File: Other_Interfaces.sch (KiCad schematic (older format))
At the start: 1 part, among them J9 2908-05WB-MG

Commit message: Add uSD circuitry
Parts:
- added C? (x2): C_100n_0402, antmicro-footprints:0402-cap, symbol antmicroCapacitors0402:C_100n_0402
- added C?: C_10u_0603, antmicro-footprints:0603-cap, symbol antmicroCapacitors0603:C_10u_0603
- added D? (x2): TPD4E05U06_PASS, antmicro-footprints:TPD4E05U06_PASS, symbol antmicroTVSDiodes:TPD4E05U06_PASS
- added IC?: AP22652W6-7, antmicro-footprints:SOT-23-6, symbol antmicroPMICPowerDistributionSwitchesLoadDrivers:AP22652W6-7
- added R?: R_20k_0402, antmicro-footprints:0402-res, symbol antmicroResistors0402:R_20k_0402
- added R?: R_10k_0402, antmicro-footprints:0402-res, symbol antmicroResistors0402:R_10k_0402
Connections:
- net labels added: 3V3, GND, SDMCC_EN, SDMCC_VDD, SDMCC_VDD_FAULT#, SDMCC_VDD_ILIM, SDMMC_CD, SDMMC_CLK, SDMMC_CMD, SDMMC_DAT0, SDMMC_DAT1, SDMMC_DAT2, SDMMC_DAT3
- wire segments 0 -> 50
- no-connect marks 0 -> 1
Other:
- note added: "Text"
- note removed: "Work in progress."
- moved on the sheet: J9

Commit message: Annotate parts in Other_Interfaces.sch
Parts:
- gave numbers to parts that had none: 8
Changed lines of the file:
@@
 Text
 $Comp
-L antmicroTVSDiodes:TPD4E05U06_PASS D?
+L antmicroTVSDiodes:TPD4E05U06_PASS D21
 U 1 1 61F2105E
 P 2450 3650
-F 0 "D?" V 2933 3600 60  0000 C CNN
+F 0 "D21" V 2933 3600 60  0000 C CNN
 F 1 "TPD4E05U06_PASS" V 3039 3600 60  0000 C CNN
 F 2 "antmicro-footprints:TPD4E05U06_PASS" H 2450 3650 60  0001 C CNN
@@
 $EndComp
 $Comp
-L antmicroTVSDiodes:TPD4E05U06_PASS D?
+L antmicroTVSDiodes:TPD4E05U06_PASS D22
 U 1 1 61F22664
 P 3375 3650
-F 0 "D?" V 3858 3600 60  0000 C CNN
+F 0 "D22" V 3858 3600 60  0000 C CNN
 F 1 "TPD4E05U06_PASS" V 3964 3600 60  0000 C CNN
 F 2 "antmicro-footprints:TPD4E05U06_PASS" H 3375 3650 60  0001 C CNN
@@
 $EndComp
 $Comp
-L antmicroPMICPowerDistributionSwitchesLoadDrivers:AP22652W6-7 IC?
+L antmicroPMICPowerDistributionSwitchesLoadDrivers:AP22652W6-7 IC2
 U 1 1 61F28646
 P 2400 1450
-F 0 "IC?" H 2400 1815 50  0000 C CNN
+F 0 "IC2" H 2400 1815 50  0000 C CNN
 F 1 "AP22652W6-7" H 2400 1724 50  0000 C CNN
 F 2 "antmicro-footprints:SOT-23-6" H 2400 1200 50  0001 C CNN
@@
 P 1950 1600
 AR Path="/61A60486/61F34FAA" Ref="#PWR?"  Part="1"
-AR Path="/61C01D88/61F34FAA" Ref="#PWR?"  Part="1"
-F 0 "#PWR?" H 1950 1350 50  0001 C CNN
+AR Path="/61C01D88/61F34FAA" Ref="#PWR0184"  Part="1"
+F 0 "#PWR0184" H 1950 1350 50  0001 C CNN
 F 1 "GND" H 1955 1427 50  0000 C CNN
 F 2 "" H 1950 1600 50  0001 C CNN
@@
 	2800 1350 3175 1350
 $Comp
-L antmicroCapacitors0402:C_100n_0402 C?
+L antmicroCapacitors0402:C_100n_0402 C124
 U 1 1 61F42291
 P 1400 1500
-F 0 "C?" H 1515 1455 60  0000 L CNN
+F 0 "C124" H 1515 1455 60  0000 L CNN
 F 1 "C_100n_0402" H 1400 1350 60  0001 C CNN
 F 2 "antmicro-footprints:0402-cap" H 1600 1700 60  0001 L CNN
@@
 P 1400 1650
 AR Path="/61A60486/61F43E22" Ref="#PWR?"  Part="1"
-AR Path="/61C01D88/61F43E22" Ref="#PWR?"  Part="1"
-F 0 "#PWR?" H 1400 1400 50  0001 C CNN
+AR Path="/61C01D88/61F43E22" Ref="#PWR0185"  Part="1"
+F 0 "#PWR0185" H 1400 1400 50  0001 C CNN
 F 1 "GND" H 1405 1477 50  0000 C CNN
 F 2 "" H 1400 1650 50  0001 C CNN
@@
 	2850 1550 2850 1600
 $Comp
-L antmicroResistors0402:R_20k_0402 R?
+L antmicroResistors0402:R_20k_0402 R105
 U 1 1 61F44F3A
 P 2850 1750
-F 0 "R?" V 2805 1820 60  0000 L CNN
+F 0 "R105" V 2805 1820 60  0000 L CNN
 F 1 "R_20k_0402" H 2850 1600 60  0001 C CNN
 F 2 "antmicro-footprints:0402-res" H 3050 1950 60  0001 L CNN
@@
 P 2850 1900
 AR Path="/61A60486/61F45C55" Ref="#PWR?"  Part="1"
-AR Path="/61C01D88/61F45C55" Ref="#PWR?"  Part="1"
-F 0 "#PWR?" H 2850 1650 50  0001 C CNN
+AR Path="/61C01D88/61F45C55" Ref="#PWR0186"  Part="1"
+F 0 "#PWR0186" H 2850 1650 50  0001 C CNN
 F 1 "GND" H 2855 1727 50  0000 C CNN
 F 2 "" H 2850 1900 50  0001 C CNN
@@
 $EndComp
 $Comp
-L antmicroResistors0402:R_10k_0402 R?
+L antmicroResistors0402:R_10k_0402 R104
 U 1 1 61F474AB
 P 2850 1125
-F 0 "R?" V 2805 1195 60  0000 L CNN
+F 0 "R104" V 2805 1195 60  0000 L CNN
 F 1 "R_10k_0402" H 2850 975 60  0001 C CNN
 F 2 "antmicro-footprints:0402-res" H 3050 1325 60  0001 L CNN
@@
 	2850 925  2850 975
 $Comp
-L antmicroCapacitors0402:C_100n_0402 C?
+L antmicroCapacitors0402:C_100n_0402 C125
 U 1 1 61F4A017
 P 3175 1500
-F 0 "C?" H 3060 1455 60  0000 R CNN
+F 0 "C125" H 3060 1455 60  0000 R CNN
 F 1 "C_100n_0402" H 3175 1350 60  0001 C CNN
 F 2 "antmicro-footprints:0402-cap" H 3375 1700 60  0001 L CNN
@@
 P 3175 1650
 AR Path="/61A60486/61F4A01D" Ref="#PWR?"  Part="1"
-AR Path="/61C01D88/61F4A01D" Ref="#PWR?"  Part="1"
-F 0 "#PWR?" H 3175 1400 50  0001 C CNN
+AR Path="/61C01D88/61F4A01D" Ref="#PWR0187"  Part="1"
+F 0 "#PWR0187" H 3175 1400 50  0001 C CNN
 F 1 "GND" H 3180 1477 50  0000 C CNN
 F 2 "" H 3175 1650 50  0001 C CNN
@@
 	3175 1350 3350 1350
 $Comp
-L antmicroCapacitors0603:C_10u_0603 C?
+L antmicroCapacitors0603:C_10u_0603 C126
 U 1 1 61F4D677
 P 3650 1500
-F 0 "C?" H 3765 1545 60  0000 L CNN
+F 0 "C126" H 3765 1545 60  0000 L CNN
 F 1 "C_10u_0603" H 3650 1350 60  0001 C CNN
 F 2 "antmicro-footprints:0603-cap" H 3850 1700 60  0001 L CNN
@@
 P 3650 1650
 AR Path="/61A60486/61F4E5D5" Ref="#PWR?"  Part="1"
-AR Path="/61C01D88/61F4E5D5" Ref="#PWR?"  Part="1"
-F 0 "#PWR?" H 3650 1400 50  0001 C CNN
+AR Path="/61C01D88/61F4E5D5" Ref="#PWR0188"  Part="1"
+F 0 "#PWR0188" H 3650 1400 50  0001 C CNN
 F 1 "GND" H 3655 1477 50  0000 C CNN
 F 2 "" H 3650 1650 50  0001 C CNN
@@
 AR Path="/61B0DC30/61F53284" Ref="#FLG?"  Part="1"
 AR Path="/61DC2BE0/61F53284" Ref="#FLG?"  Part="1"
-F 0 "#FLG?" H 3350 1425 50  0001 C CNN
+AR Path="/61C01D88/61F53284" Ref="#FLG0107"  Part="1"
+F 0 "#FLG0107" H 3350 1425 50  0001 C CNN
 F 1 "PWR_FLAG" H 3350 1523 50  0000 C CNN
 F 2 "" H 3350 1350 50  0001 C CNN
@@
 P 1950 3575
 AR Path="/61A60486/61F64597" Ref="#PWR?"  Part="1"
-AR Path="/61C01D88/61F64597" Ref="#PWR?"  Part="1"
-F 0 "#PWR?" H 1950 3325 50  0001 C CNN
+AR Path="/61C01D88/61F64597" Ref="#PWR0189"  Part="1"
+F 0 "#PWR0189" H 1950 3325 50  0001 C CNN
 F 1 "GND" H 1955 3402 50  0000 C CNN
 F 2 "" H 1950 3575 50  0001 C CNN
@@
 P 2875 3575
 AR Path="/61A60486/61F649BB" Ref="#PWR?"  Part="1"
-AR Path="/61C01D88/61F649BB" Ref="#PWR?"  Part="1"
-F 0 "#PWR?" H 2875 3325 50  0001 C CNN
+AR Path="/61C01D88/61F649BB" Ref="#PWR0190"  Part="1"
+F 0 "#PWR0190" H 2875 3325 50  0001 C CNN
 F 1 "GND" H 2880 3402 50  0000 C CNN
 F 2 "" H 2875 3575 50  0001 C CNN
@@
 P 4050 3350
 AR Path="/61A60486/61F78331" Ref="#PWR?"  Part="1"
-AR Path="/61C01D88/61F78331" Ref="#PWR?"  Part="1"
-F 0 "#PWR?" H 4050 3100 50  0001 C CNN
+AR Path="/61C01D88/61F78331" Ref="#PWR0191"  Part="1"
+F 0 "#PWR0191" H 4050 3100 50  0001 C CNN
 F 1 "GND" H 4055 3177 50  0000 C CNN
 F 2 "" H 4050 3350 50  0001 C CNN

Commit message: Connect uSD to SOM
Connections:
- net labels added: SD_CLK, SD_CMD, SD_DATA0, SD_DATA1, SD_DATA2, SD_DATA3, SD_DET
- net labels removed: SDMMC_CD, SDMMC_CLK, SDMMC_CMD, SDMMC_DAT0, SDMMC_DAT1, SDMMC_DAT2, SDMMC_DAT3
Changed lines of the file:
@@
 	1    0    0    -1
 $EndComp
-Text GLabel 1625 3200 0    50   Input ~ 0
-SDMMC_DAT1
-Text GLabel 1625 3100 0    50   Input ~ 0
-SDMMC_DAT0
-Text GLabel 1625 2500 0    50   Input ~ 0
-SDMMC_DAT2
-Text GLabel 1625 2600 0    50   Input ~ 0
-SDMMC_DAT3
-Text GLabel 1625 2700 0    50   Input ~ 0
-SDMMC_CMD
-Text GLabel 1625 2900 0    50   Input ~ 0
-SDMMC_CLK
-Text GLabel 1625 2400 0    50   Input ~ 0
-SDMMC_CD
 Wire Wire Line
 	4100 3300 4050 3300
@@
 Wire Wire Line
 	3350 1350 3650 1350
+Text GLabel 1625 2900 0    50   Input ~ 0
+SD_CLK
+Text GLabel 1625 2700 0    50   Input ~ 0
+SD_CMD
+Text GLabel 1625 2400 0    50   Input ~ 0
+SD_DET
+Text GLabel 1625 3100 0    50   Input ~ 0
+SD_DATA0
+Text GLabel 1625 3200 0    50   Input ~ 0
+SD_DATA1
+Text GLabel 1625 2600 0    50   Input ~ 0
+SD_DATA3
+Text GLabel 1625 2500 0    50   Input ~ 0
+SD_DATA2
 $EndSCHEMATC

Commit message: Add USB debug circuitry, loclib
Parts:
- C124, C125: footprint antmicro-footprints:0402-cap -> sa800u-baseboard-hw-footprints:0402-cap; symbol antmicroCapacitors0402:C_100n_0402 -> sa800u-baseboard-hw:C_100n_0402
- C126: footprint antmicro-footprints:0603-cap -> sa800u-baseboard-hw-footprints:0603-cap; symbol antmicroCapacitors0603:C_10u_0603 -> sa800u-baseboard-hw:C_10u_0603
- D21, D22: footprint antmicro-footprints:TPD4E05U06_PASS -> sa800u-baseboard-hw-footprints:TPD4E05U06_PASS; symbol antmicroTVSDiodes:TPD4E05U06_PASS -> sa800u-baseboard-hw:TPD4E05U06_PASS
- IC2: footprint antmicro-footprints:SOT-23-6 -> sa800u-baseboard-hw-footprints:SOT-23-6; symbol antmicroPMICPowerDistributionSwitchesLoadDrivers:AP22652W6-7 -> sa800u-baseboard-hw:AP22652W6-7
- R104: footprint antmicro-footprints:0402-res -> sa800u-baseboard-hw-footprints:0402-res; symbol antmicroResistors0402:R_10k_0402 -> sa800u-baseboard-hw:R_10k_0402
- R105: footprint antmicro-footprints:0402-res -> sa800u-baseboard-hw-footprints:0402-res; symbol antmicroResistors0402:R_20k_0402 -> sa800u-baseboard-hw:R_20k_0402
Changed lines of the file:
@@
 Text
 $Comp
-L antmicroTVSDiodes:TPD4E05U06_PASS D21
+L sa800u-baseboard-hw:TPD4E05U06_PASS D21
 U 1 1 61F2105E
 P 2450 3650
 F 0 "D21" V 2933 3600 60  0000 C CNN
 F 1 "TPD4E05U06_PASS" V 3039 3600 60  0000 C CNN
-F 2 "antmicro-footprints:TPD4E05U06_PASS" H 2450 3650 60  0001 C CNN
+F 2 "sa800u-baseboard-hw-footprints:TPD4E05U06_PASS" H 2450 3650 60  0001 C CNN
 F 3 "" H 2450 3650 60  0001 C CNN
 F 4 "Texas Instruments" H 2450 3650 50  0001 C CNN "Manufacturer"
@@
 $EndComp
 $Comp
-L antmicroTVSDiodes:TPD4E05U06_PASS D22
+L sa800u-baseboard-hw:TPD4E05U06_PASS D22
 U 1 1 61F22664
 P 3375 3650
 F 0 "D22" V 3858 3600 60  0000 C CNN
 F 1 "TPD4E05U06_PASS" V 3964 3600 60  0000 C CNN
-F 2 "antmicro-footprints:TPD4E05U06_PASS" H 3375 3650 60  0001 C CNN
+F 2 "sa800u-baseboard-hw-footprints:TPD4E05U06_PASS" H 3375 3650 60  0001 C CNN
 F 3 "" H 3375 3650 60  0001 C CNN
 F 4 "Texas Instruments" H 3375 3650 50  0001 C CNN "Manufacturer"
@@
 $EndComp
 $Comp
-L antmicroPMICPowerDistributionSwitchesLoadDrivers:AP22652W6-7 IC2
+L sa800u-baseboard-hw:AP22652W6-7 IC2
 U 1 1 61F28646
 P 2400 1450
 F 0 "IC2" H 2400 1815 50  0000 C CNN
 F 1 "AP22652W6-7" H 2400 1724 50  0000 C CNN
-F 2 "antmicro-footprints:SOT-23-6" H 2400 1200 50  0001 C CNN
+F 2 "sa800u-baseboard-hw-footprints:SOT-23-6" H 2400 1200 50  0001 C CNN
 F 3 "https://www.diodes.com/assets/Datasheets/AP22652_53_52A_53A.pdf" H 2400 1450 50  0001 C CNN
 F 4 "Diodes Incorporated " H 2400 1100 50  0001 C CNN "Manufacturer"
@@
 	2800 1350 3175 1350
 $Comp
-L antmicroCapacitors0402:C_100n_0402 C124
+L sa800u-baseboard-hw:C_100n_0402 C124
 U 1 1 61F42291
 P 1400 1500
 F 0 "C124" H 1515 1455 60  0000 L CNN
 F 1 "C_100n_0402" H 1400 1350 60  0001 C CNN
-F 2 "antmicro-footprints:0402-cap" H 1600 1700 60  0001 L CNN
+F 2 "sa800u-baseboard-hw-footprints:0402-cap" H 1600 1700 60  0001 L CNN
 F 3 "" H 1400 1500 50  0001 C CNN
 F 4 "Murata" H 1600 1900 60  0001 L CNN "Manufacturer"
@@
 	2850 1550 2850 1600
 $Comp
-L antmicroResistors0402:R_20k_0402 R105
+L sa800u-baseboard-hw:R_20k_0402 R105
 U 1 1 61F44F3A
 P 2850 1750
 F 0 "R105" V 2805 1820 60  0000 L CNN
 F 1 "R_20k_0402" H 2850 1600 60  0001 C CNN
-F 2 "antmicro-footprints:0402-res" H 3050 1950 60  0001 L CNN
+F 2 "sa800u-baseboard-hw-footprints:0402-res" H 3050 1950 60  0001 L CNN
 F 3 "" H 2850 1750 50  0001 C CNN
 F 4 "VISHAY" H 3050 2150 60  0001 L CNN "Manufacturer"
@@
 $EndComp
 $Comp
-L antmicroResistors0402:R_10k_0402 R104
+L sa800u-baseboard-hw:R_10k_0402 R104
 U 1 1 61F474AB
 P 2850 1125
 F 0 "R104" V 2805 1195 60  0000 L CNN
 F 1 "R_10k_0402" H 2850 975 60  0001 C CNN
-F 2 "antmicro-footprints:0402-res" H 3050 1325 60  0001 L CNN
+F 2 "sa800u-baseboard-hw-footprints:0402-res" H 3050 1325 60  0001 L CNN
 F 3 "" H 2850 1125 50  0001 C CNN
 F 4 "VISHAY" H 3050 1525 60  0001 L CNN "Manufacturer"
@@
 	2850 925  2850 975
 $Comp
-L antmicroCapacitors0402:C_100n_0402 C125
+L sa800u-baseboard-hw:C_100n_0402 C125
 U 1 1 61F4A017
 P 3175 1500
 F 0 "C125" H 3060 1455 60  0000 R CNN
 F 1 "C_100n_0402" H 3175 1350 60  0001 C CNN
-F 2 "antmicro-footprints:0402-cap" H 3375 1700 60  0001 L CNN
+F 2 "sa800u-baseboard-hw-footprints:0402-cap" H 3375 1700 60  0001 L CNN
 F 3 "" H 3175 1500 50  0001 C CNN
 F 4 "Murata" H 3375 1900 60  0001 L CNN "Manufacturer"
@@
 	3175 1350 3350 1350
 $Comp
-L antmicroCapacitors0603:C_10u_0603 C126
+L sa800u-baseboard-hw:C_10u_0603 C126
 U 1 1 61F4D677
 P 3650 1500
 F 0 "C126" H 3765 1545 60  0000 L CNN
 F 1 "C_10u_0603" H 3650 1350 60  0001 C CNN
-F 2 "antmicro-footprints:0603-cap" H 3850 1700 60  0001 L CNN
+F 2 "sa800u-baseboard-hw-footprints:0603-cap" H 3850 1700 60  0001 L CNN
 F 3 "" H 3650 1500 50  0001 C CNN
 F 4 "Murata" H 3850 1900 60  0001 L CNN "Manufacturer"
@@
 SDMCC_VDD
 $Comp
-L power:PWR_FLAG #FLG?
+L sa800u-baseboard-hw:PWR_FLAG #FLG?
 U 1 1 61F53284
 P 3350 1350

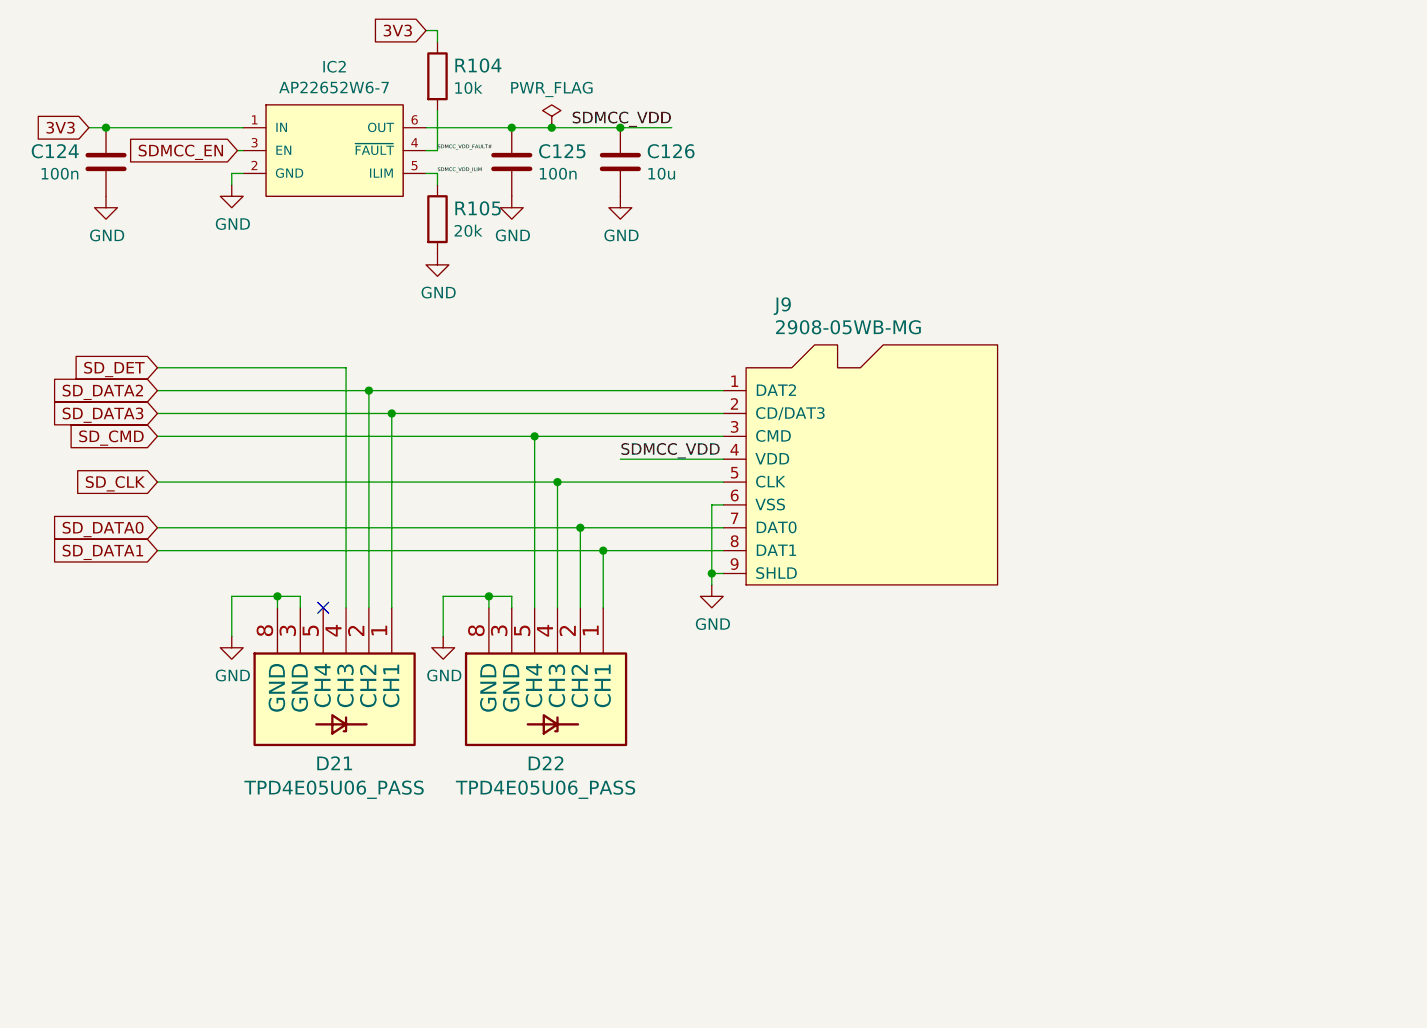
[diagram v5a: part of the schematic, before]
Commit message: Update SD circuitry to match ref design
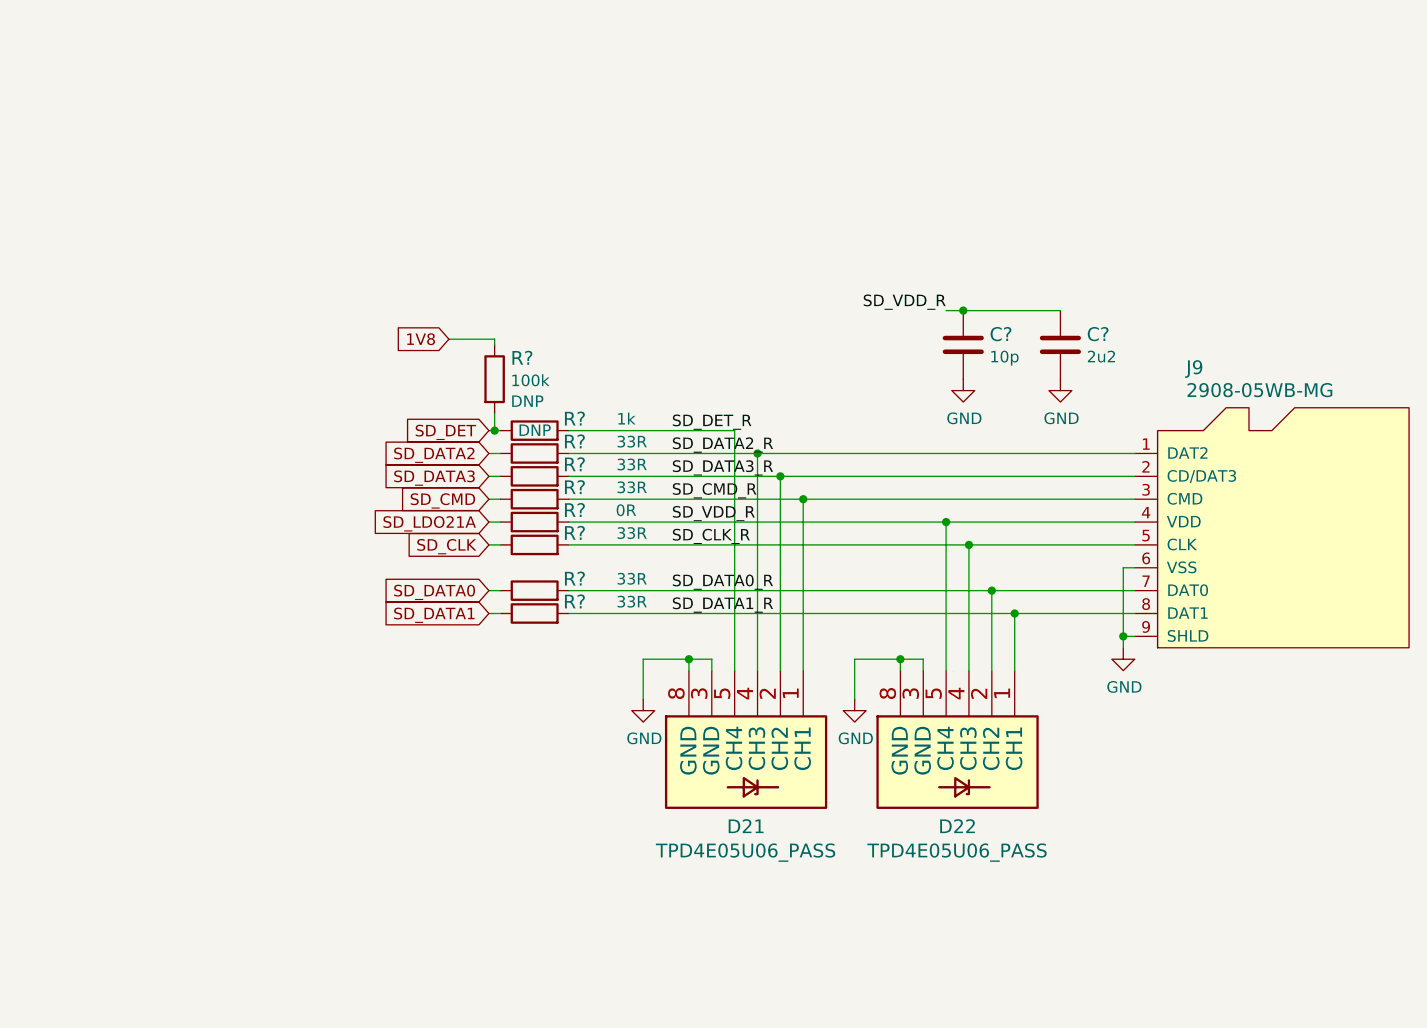
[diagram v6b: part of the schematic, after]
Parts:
- removed C124, C125: C_100n_0402, sa800u-baseboard-hw-footprints:0402-cap, symbol sa800u-baseboard-hw:C_100n_0402
- removed C126: C_10u_0603, sa800u-baseboard-hw-footprints:0603-cap, symbol sa800u-baseboard-hw:C_10u_0603
- removed IC2: AP22652W6-7, sa800u-baseboard-hw-footprints:SOT-23-6, symbol sa800u-baseboard-hw:AP22652W6-7
- removed R104: R_10k_0402, sa800u-baseboard-hw-footprints:0402-res, symbol sa800u-baseboard-hw:R_10k_0402
- removed R105: R_20k_0402, sa800u-baseboard-hw-footprints:0402-res, symbol sa800u-baseboard-hw:R_20k_0402
- added C?: C_10p_0402, sa800u-baseboard-hw-footprints:0402-cap, symbol sa800u-baseboard-hw:C_10p_0402
- added C?: C_2u2_0603, antmicro-footprints:0603-cap, symbol antmicroCapacitors0603:C_2u2_0603
- added R? (x6): R_33R_0402, antmicro-footprints:0402-res, symbol antmicroResistors0402:R_33R_0402
- added R?: R_1k_0402, sa800u-baseboard-hw-footprints:0402-res, symbol sa800u-baseboard-hw:R_1k_0402
- added R?: R_0R_0402, antmicro-footprints:0402-res, symbol antmicroResistors0402:R_0R_0402
- added R?: R_100k_0402, sa800u-baseboard-hw-footprints:0402-res, symbol sa800u-baseboard-hw:R_100k_0402
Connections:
- net GND: now also C?.2, C?.2
- net SD_CLK: now also R?.1; no longer D22.4 (CH3), J9.5 (CLK)
- net SD_CMD: now also R?.1; no longer D22.5 (CH4), J9.3 (CMD)
- net SD_DATA0: now also R?.1; no longer D22.2 (CH2), J9.7 (DAT0)
- net SD_DATA1: now also R?.1; no longer D22.1 (CH1), J9.8 (DAT1)
- net SD_DATA2: now also R?.1; no longer D21.2 (CH2), J9.1 (DAT2)
- net SD_DATA3: now also R?.1; no longer D21.1 (CH1), J9.2 (CD/DAT3)
- net SD_DET: now also R?.1, R?.2; no longer D21.4 (CH3)
- net SD_DET_R: now reaches D21.5 (CH4)
- net SD_DET_R: now also R?.2
- net SDMCC_VDD renamed SD_VDD_R
- net SD_VDD_R: now also D22.5 (CH4), C?.1, C?.1, R?.2
- new net 1V8: R?.1
- new net SD_CLK_R: D22.4 (CH3), J9.5 (CLK), R?.2
- new net SD_CMD_R: D21.1 (CH1), J9.3 (CMD), R?.2
- new net SD_DATA0_R: D22.2 (CH2), J9.7 (DAT0), R?.2
- new net SD_DATA1_R: D22.1 (CH1), J9.8 (DAT1), R?.2
- new net SD_DATA2_R: D21.4 (CH3), J9.1 (DAT2), R?.2
- new net SD_DATA3_R: D21.2 (CH2), J9.2 (CD/DAT3), R?.2
- new net SD_LDO21A: R?.1
- no-connect marks 1 -> 0
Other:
- moved on the sheet: D21, D22, J9
